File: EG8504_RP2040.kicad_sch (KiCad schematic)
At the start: 1 part, among them U1 RP2040

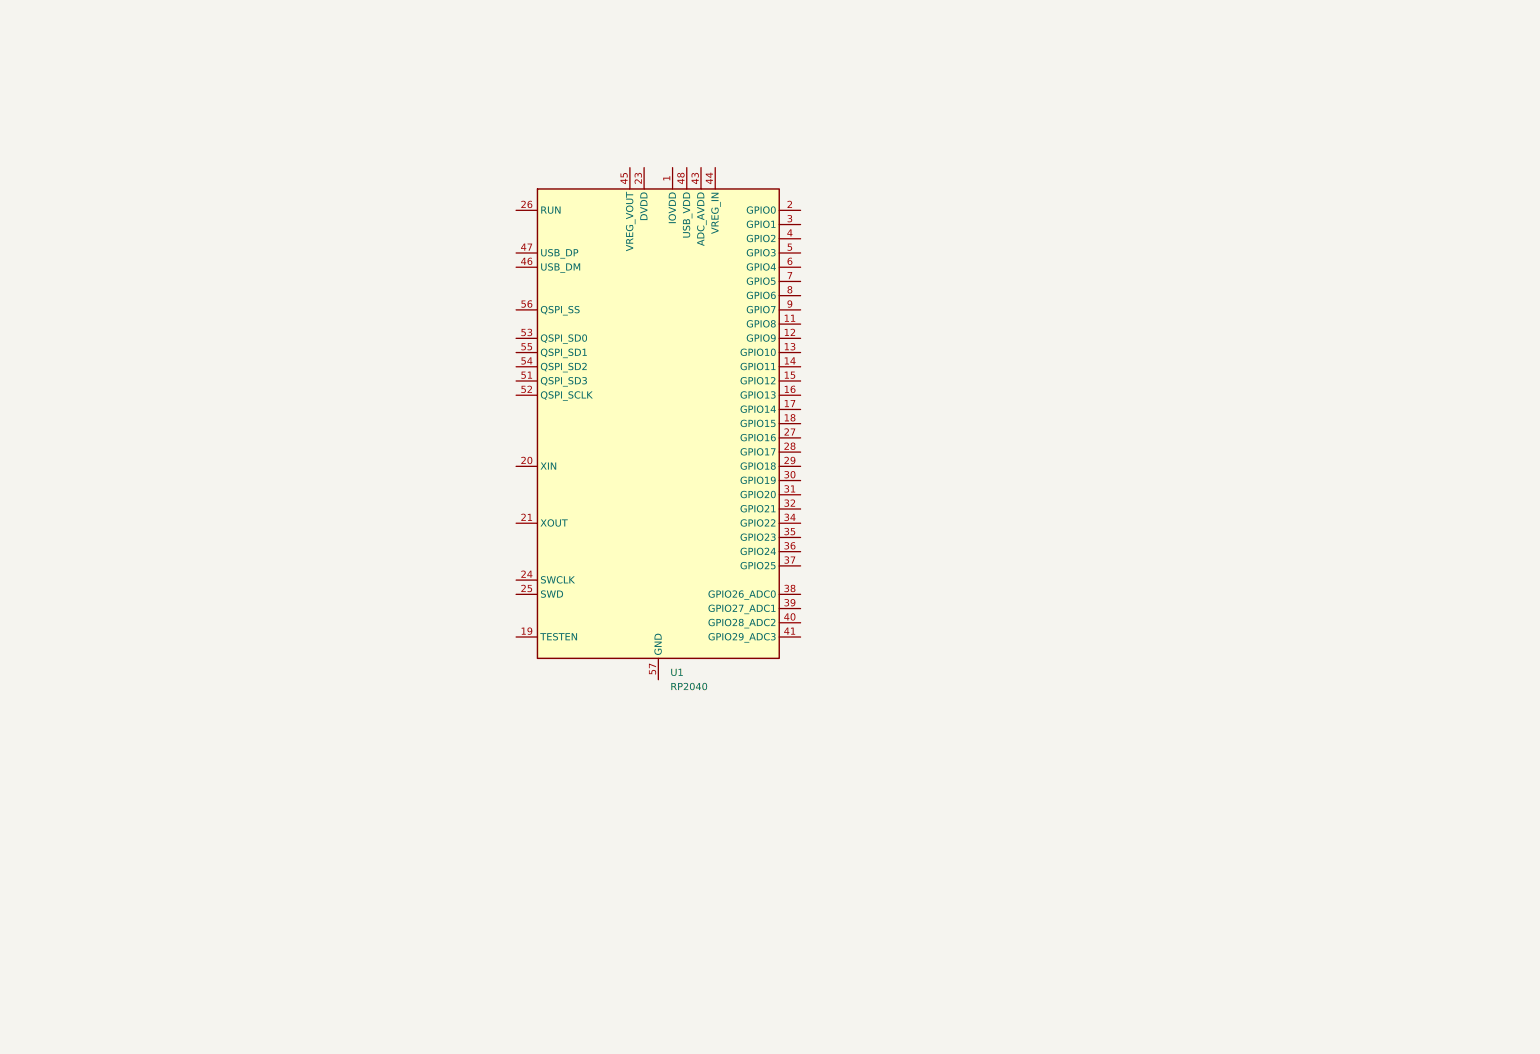
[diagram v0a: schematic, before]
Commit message: rp2040周りの部品配線を追加
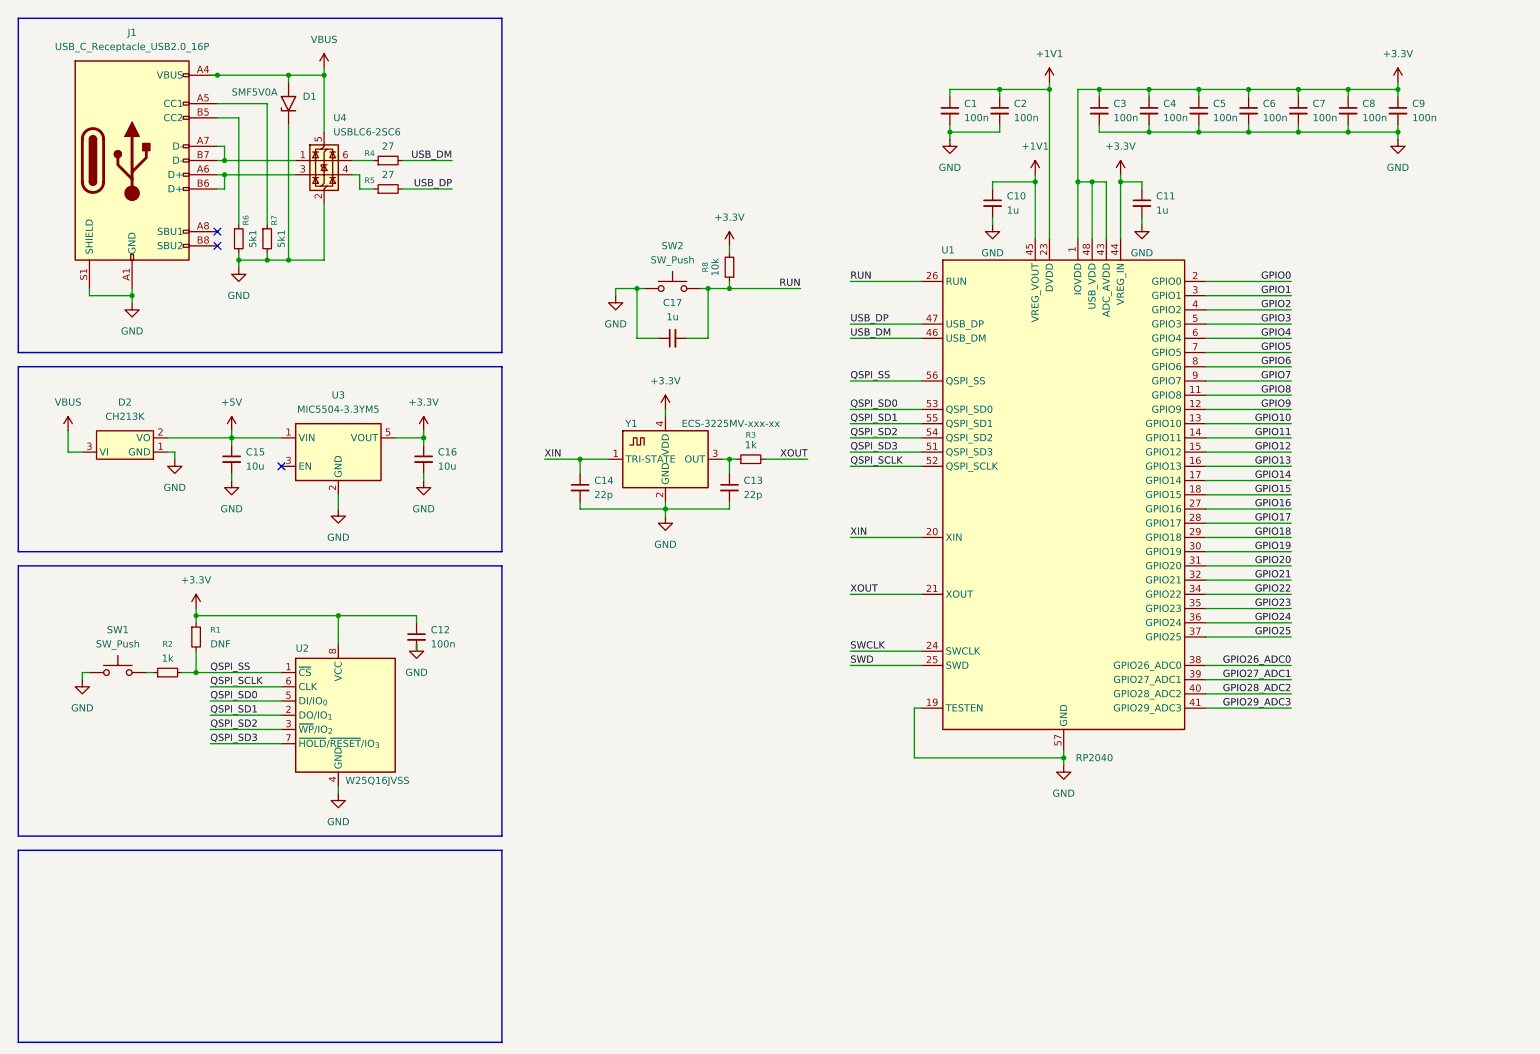
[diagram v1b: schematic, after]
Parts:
- added C1, C12, C2, C3, C4, C5, C6, C7, C8, C9: 100n, symbol Device:C_Small
- added C10, C11, C17: 1u, symbol Device:C_Small
- added C13, C14: 22p, symbol Device:C_Small
- added C15, C16: 10u, symbol Device:C_Small
- added D1: SMF5V0A, Diode_SMD:D_SMF, symbol Diode:SMF5V0A
- added D2: CH213K, symbol MyLibrary:CH213K
- added J1: USB_C_Receptacle_USB2.0_16P, symbol Connector:USB_C_Receptacle_USB2.0_16P
- added R1: DNF, symbol Device:R_Small
- added R2, R3: 1k, symbol Device:R_Small
- added R4, R5: 27, symbol Device:R_Small
- added R6, R7: 5k1, symbol Device:R_Small
- added R8: 10k, symbol Device:R_Small
- added SW1, SW2: SW_Push, symbol Switch:SW_Push
- added U2: W25Q16JVSS, Package_SO:SOIC-8_5.3x5.3mm_P1.27mm, symbol Memory_Flash:W25Q16JVSS
- added U3: MIC5504-3.3YM5, Package_TO_SOT_SMD:SOT-23-5, symbol Regulator_Linear:MIC5504-3.3YM5
- added U4: USBLC6-2SC6, Package_TO_SOT_SMD:SOT-23-6, symbol Power_Protection:USBLC6-2SC6
- added Y1: ECS-3225MV-xxx-xx, symbol MyLibrary:ECS-3225MV-xxx-xx
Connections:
- net +3.3V: now reaches U1.1 (IOVDD), U1.10 (IOVDD), U1.22 (IOVDD), U1.33 (IOVDD), U1.42 (IOVDD), U1.49 (IOVDD)
- net +3.3V: now also U1.43 (ADC_AVDD), U1.44 (VREG_IN), U1.48 (USB_VDD), C11.1, C12.1, C16.1, C3.1, C4.1, C5.1, C6.1, C7.1, C8.1, C9.1, R1.1, R8.2, U2.8 (VCC), U3.5 (VOUT), Y1.4 (VDD)
- net GPIO8: now reaches U1.11 (GPIO8)
- net GPIO9: now reaches U1.12 (GPIO9)
- net GPIO10: now reaches U1.13 (GPIO10)
- net GPIO11: now reaches U1.14 (GPIO11)
- net GPIO12: now reaches U1.15 (GPIO12)
- net GPIO13: now reaches U1.16 (GPIO13)
- net GPIO14: now reaches U1.17 (GPIO14)
- net GPIO15: now reaches U1.18 (GPIO15)
- net GND: now reaches U1.19 (TESTEN)
- net GND: now also U1.57 (GND), C1.2, C10.2, C11.2, C12.2, C13.2, C14.2, C15.2, C16.2, C17.1, C2.2, C3.2, C4.2, C5.2, C6.2, C7.2, C8.2, C9.2, D1.1 (A1), D2.1 (GND), J1.A1 (GND), J1.A12 (GND), J1.B1 (GND), J1.B12 (GND), J1.S1 (SHIELD), R6.2, R7.2, SW1.1, SW2.1, U2.4 (GND), U3.2 (GND), U4.2 (GND), Y1.2 (GND)
- net GPIO0: now reaches U1.2 (GPIO0)
- net XIN: now reaches U1.20 (XIN)
- net XIN: now also C14.1, Y1.1 (TRI-STATE)
- net XOUT: now reaches U1.21 (XOUT)
- net XOUT: now also R3.2
- net +1V1: now reaches U1.23 (DVDD), U1.50 (DVDD)
- net +1V1: now also U1.45 (VREG_VOUT), C1.1, C10.1, C2.1
- net SWCLK: now reaches U1.24 (SWCLK)
- net SWD: now reaches U1.25 (SWD)
- net RUN: now reaches U1.26 (RUN)
- net RUN: now also C17.2, R8.1, SW2.2
- net GPIO16: now reaches U1.27 (GPIO16)
- net GPIO17: now reaches U1.28 (GPIO17)
- net GPIO18: now reaches U1.29 (GPIO18)
- net GPIO1: now reaches U1.3 (GPIO1)
- net GPIO19: now reaches U1.30 (GPIO19)
- net GPIO20: now reaches U1.31 (GPIO20)
- net GPIO21: now reaches U1.32 (GPIO21)
- net GPIO22: now reaches U1.34 (GPIO22)
- net GPIO23: now reaches U1.35 (GPIO23)
- net GPIO24: now reaches U1.36 (GPIO24)
- net GPIO25: now reaches U1.37 (GPIO25)
- net GPIO26_ADC0: now reaches U1.38 (GPIO26_ADC0)
- net GPIO27_ADC1: now reaches U1.39 (GPIO27_ADC1)
- net GPIO2: now reaches U1.4 (GPIO2)
- net GPIO28_ADC2: now reaches U1.40 (GPIO28_ADC2)
- net GPIO29_ADC3: now reaches U1.41 (GPIO29_ADC3)
- net USB_DM: now reaches U1.46 (USB_DM)
- net USB_DM: now also R4.2
- net USB_DP: now reaches U1.47 (USB_DP)
- net USB_DP: now also R5.2
- net GPIO3: now reaches U1.5 (GPIO3)
- net QSPI_SD3: now reaches U1.51 (QSPI_SD3)
- net QSPI_SD3: now also U2.7 (~{HOLD}/~{RESET}/IO_{3})
- net QSPI_SCLK: now reaches U1.52 (QSPI_SCLK)
- net QSPI_SCLK: now also U2.6 (CLK)
- net QSPI_SD0: now reaches U1.53 (QSPI_SD0)
- net QSPI_SD0: now also U2.5 (DI/IO_{0})
- net QSPI_SD2: now reaches U1.54 (QSPI_SD2)
- net QSPI_SD2: now also U2.3 (~{WP}/IO_{2})
- net QSPI_SD1: now reaches U1.55 (QSPI_SD1)
- net QSPI_SD1: now also U2.2 (DO/IO_{1})
- net QSPI_SS: now reaches U1.56 (QSPI_SS)
- net QSPI_SS: now also R1.2, R2.2, U2.1 (~{CS})
- net GPIO4: now reaches U1.6 (GPIO4)
- net GPIO5: now reaches U1.7 (GPIO5)
- net GPIO6: now reaches U1.8 (GPIO6)
- net GPIO7: now reaches U1.9 (GPIO7)
- new net: C13.1, R3.1, Y1.3 (OUT)
- new net: R2.1, SW1.2
- new net: J1.A7 (D-), J1.B7 (D-), U4.1 (I/O1)
- new net: J1.A6 (D+), J1.B6 (D+), U4.3 (I/O2)
- new net: R5.1, U4.4 (I/O2)
- new net: R4.1, U4.6 (I/O1)
- new net: J1.A5 (CC1), R7.1
- new net: J1.B5 (CC2), R6.1
- new net +5V: C15.1, D2.2 (VO), U3.1 (VIN)
- new net VBUS: D1.2 (A2), D2.3 (VI), J1.A4 (VBUS), J1.A9 (VBUS), J1.B4 (VBUS), J1.B9 (VBUS), U4.5 (VBUS)
- no-connect marks 0 -> 3
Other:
- moved on the sheet: U1

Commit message: EG8504用のDCDCを追加
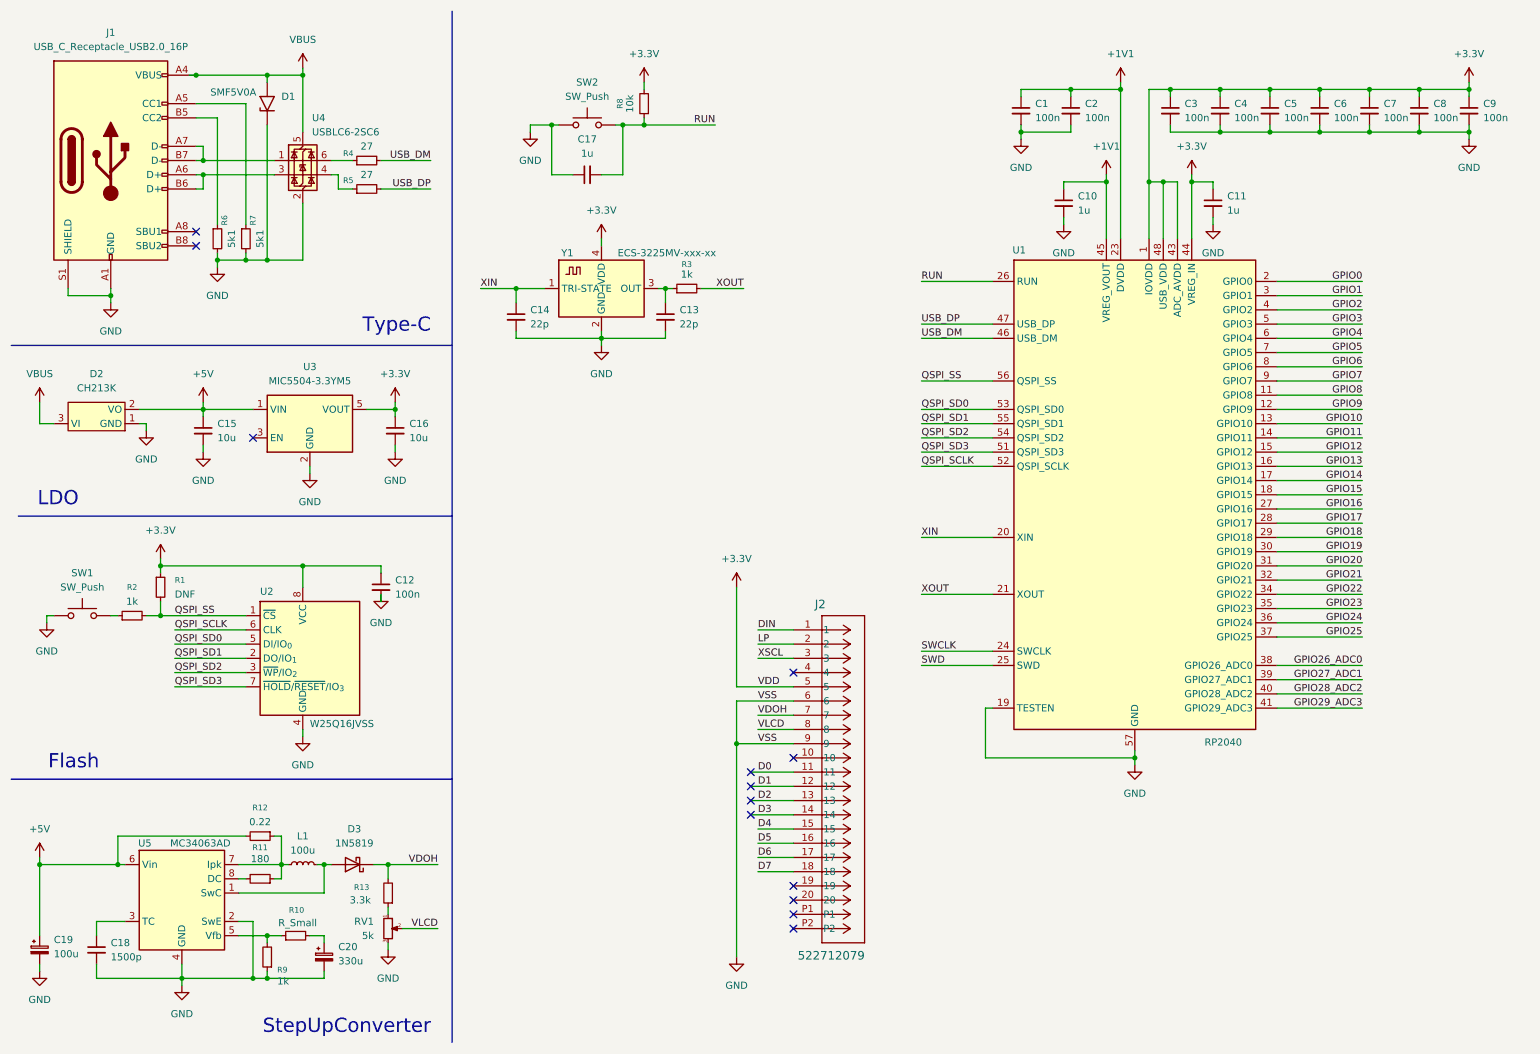
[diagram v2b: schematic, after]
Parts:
- added C18: 1500p, symbol Device:C_Small
- added C19: 100u, symbol Device:C_Polarized_Small
- added C20: 330u, symbol Device:C_Polarized_Small
- added D3: 1N5819, Diode_THT:D_DO-41_SOD81_P10.16mm_Horizontal, symbol Diode:1N5819
- added J2: 522712079, MyLibrary:CON_522712079_MOL, symbol MyLibrary:522712079
- added L1: 100u, symbol Device:L_Small
- added R10: R_Small, symbol Device:R_Small
- added R11: 180, symbol Device:R_Small
- added R12: 0.22, symbol Device:R_Small
- added R13: 3.3k, symbol Device:R_Small
- added R9: 1k, symbol Device:R_Small
- added RV1: 5k, symbol Device:R_Potentiometer_Small
- added U5: MC34063AD, Package_SO:SOIC-8_3.9x4.9mm_P1.27mm, symbol Regulator_Switching:MC34063AD
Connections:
- net +3.3V: now also J2.5
- net +5V: now also C19.1, R12.2, U5.6 (Vin)
- net GND: now also C18.2, C19.2, C20.2, J2.6, J2.9, R9.1, RV1.3, U5.2 (SwE), U5.4 (GND)
- new net: L1.1, R11.1, R12.1, U5.7 (Ipk)
- new net: R11.2, U5.8 (DC)
- new net: D3.2 (A), L1.2, U5.1 (SwC)
- new net: C18.1, U5.3 (TC)
- new net: R10.1, R9.2, U5.5 (Vfb)
- new net: R13.1, RV1.1
- new net: C20.1, R10.2
- new net D0: J2.11
- new net D1: J2.12
- new net D2: J2.13
- new net D3: J2.14
- new net D4: J2.15
- new net D5: J2.16
- new net D6: J2.17
- new net D7: J2.18
- new net DIN: J2.1
- new net LP: J2.2
- new net VDOH: D3.1 (K), J2.7, R13.2
- new net VLCD: J2.8, RV1.2
- new net XSCL: J2.3
- no-connect marks 3 -> 13
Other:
- note added: "Flash"
- note added: "LDO"
- note added: "StepUpConverter"
- note added: "Type-C"
- moved on the sheet: C1, C10, C11, C12, C13, C14, C15, C16, C17, C2, C3, C4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

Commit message: コネクタの配置とPCB
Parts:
- added D4: LED_Small, LED_SMD:LED_0603_1608Metric_Pad1.05x0.95mm_HandSolder, symbol Device:LED_Small
- added J3, J4, J5: Conn_01x03_Socket, Connector_PinHeader_2.54mm:PinHeader_1x03_P2.54mm_Vertical, symbol Connector:Conn_01x03_Socket
- added J6, J7: Conn_01x20_Socket, Connector_PinHeader_2.54mm:PinHeader_1x20_P2.54mm_Vertical, symbol Connector:Conn_01x20_Socket
- added R14: 1k, Resistor_SMD:R_0603_1608Metric_Pad0.98x0.95mm_HandSolder, symbol Device:R_Small
- C1, C10, C11, C12, C13, C14, C15, C16, C17, C18, C2, C3, C4, C5, C6, C7, C8, C9: footprint (none) -> Capacitor_SMD:C_0603_1608Metric_Pad1.08x0.95mm_HandSolder
- C19, C20: footprint (none) -> MyLibrary:CP_Radial_D8.0mm_P3.50mm_P5.00mm
- D2: footprint (none) -> Package_TO_SOT_SMD:SOT-23_Handsoldering
- J1: footprint (none) -> Connector_USB:USB_C_Receptacle_GCT_USB4105-xx-A_16P_TopMnt_Horizontal
- R1, R11, R12, R13, R2, R3, R4, R5, R6, R7, R8, R9: footprint (none) -> Resistor_SMD:R_0603_1608Metric_Pad0.98x0.95mm_HandSolder
- R10: value R_Small -> 15k; footprint (none) -> Resistor_SMD:R_0603_1608Metric_Pad0.98x0.95mm_HandSolder
- SW1, SW2: footprint (none) -> Button_Switch_SMD:SW_Push_1P1T_NO_Vertical_Wuerth_434133025816
- Y1: footprint (none) -> Crystal:Crystal_SMD_3225-4Pin_3.2x2.5mm_HandSoldering
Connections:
- net +3.3V: now also J4.3 (Pin_3), J7.2 (Pin_2)
- net +5V: now also J4.1 (Pin_1), J7.1 (Pin_1)
- net GND: now also J3.2 (Pin_2), J4.2 (Pin_2), J5.2 (Pin_2), J6.13 (Pin_13), J6.18 (Pin_18), J6.3 (Pin_3), J7.13 (Pin_13), J7.18 (Pin_18), J7.3 (Pin_3), J7.8 (Pin_8), R14.1
- net GPIO0: now also J3.1 (Pin_1), J6.1 (Pin_1)
- net GPIO1: now also J3.3 (Pin_3), J6.2 (Pin_2)
- net GPIO10: now also J6.14 (Pin_14)
- net GPIO11: now also J6.15 (Pin_15)
- net GPIO12: now also J6.16 (Pin_16)
- net GPIO13: now also J6.17 (Pin_17)
- net GPIO14: now also J6.19 (Pin_19)
- net GPIO15: now also J6.20 (Pin_20)
- net GPIO16: now also J7.20 (Pin_20)
- net GPIO17: now also J7.19 (Pin_19)
- net GPIO18: now also J7.17 (Pin_17)
- net GPIO19: now also J7.16 (Pin_16)
- net GPIO2: now also J6.4 (Pin_4)
- net GPIO20: now also J7.15 (Pin_15)
- net GPIO21: now also J7.14 (Pin_14)
- net GPIO22: now also J7.12 (Pin_12)
- net GPIO23: now also J7.11 (Pin_11)
- net GPIO24: now also J7.10 (Pin_10)
- net GPIO25: now also D4.2 (A), J7.9 (Pin_9)
- net GPIO26_ADC0: now also J7.7 (Pin_7)
- net GPIO27_ADC1: now also J7.6 (Pin_6)
- net GPIO28_ADC2: now also J7.5 (Pin_5)
- net GPIO29_ADC3: now also J7.4 (Pin_4)
- net GPIO3: now also J6.5 (Pin_5)
- net GPIO4: now also J6.6 (Pin_6)
- net GPIO5: now also J6.7 (Pin_7)
- net GPIO6: now also J6.9 (Pin_9)
- net GPIO7: now also J6.10 (Pin_10)
- net GPIO8: now also J6.11 (Pin_11)
- net GPIO9: now also J6.12 (Pin_12)
- net RUN: now also J6.8 (Pin_8)
- net SWCLK: now also J5.3 (Pin_3)
- net SWD: now also J5.1 (Pin_1)
- new net: D4.1 (K), R14.2
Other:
- moved on the sheet: C1, C10, C11, C13, C14, C17, C2, C3, C4, C5, C6, C7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

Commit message: マイコン回りの配線
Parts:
- removed C17: 1u, Capacitor_SMD:C_0603_1608Metric_Pad1.08x0.95mm_HandSolder, symbol Device:C_Small
- removed J4, J5: Conn_01x03_Socket, Connector_PinHeader_2.54mm:PinHeader_1x03_P2.54mm_Vertical, symbol Connector:Conn_01x03_Socket
- removed J6, J7: Conn_01x20_Socket, Connector_PinHeader_2.54mm:PinHeader_1x20_P2.54mm_Vertical, symbol Connector:Conn_01x20_Socket
- added J4, J5: Conn_01x14_Socket, Connector_PinHeader_2.54mm:PinHeader_1x14_P2.54mm_Vertical, symbol Connector:Conn_01x14_Socket
- C19: footprint MyLibrary:CP_Radial_D8.0mm_P3.50mm_P5.00mm -> Capacitor_SMD:CP_Elec_6.3x5.4
- C20: footprint MyLibrary:CP_Radial_D8.0mm_P3.50mm_P5.00mm -> Capacitor_SMD:CP_Elec_10x10.5
- R1: now not fitted
- RV1: footprint (none) -> Potentiometer_THT:Potentiometer_Vishay_T73YP_Vertical
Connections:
- net GPIO13 is gone; now on net DIN: U1.16 (GPIO13)
- net GPIO16 is gone; now on net D4: U1.27 (GPIO16)
- net GPIO17 is gone; now on net D5: U1.28 (GPIO17)
- net GPIO18 is gone; now on net D6: U1.29 (GPIO18)
- net GPIO19 is gone; now on net D7: U1.30 (GPIO19)
- net LP is gone; now on net GPIO14: J2.2
- net XSCL is gone; now on net GPIO15: J2.3
- net +3.3V: now also J4.1 (Pin_1)
- net +5V: now also J5.1 (Pin_1)
- net GND: now also J5.14 (Pin_14), J5.2 (Pin_2)
- net GPIO0: now also J4.2 (Pin_2); no longer J3.1 (Pin_1)
- net GPIO1: now also J4.3 (Pin_3); no longer J3.3 (Pin_3)
- net GPIO10: now also J4.12 (Pin_12)
- net GPIO11: now also J4.13 (Pin_13)
- net GPIO12: now also J4.14 (Pin_14)
- net GPIO2: now also J4.4 (Pin_4)
- net GPIO20: now also J5.12 (Pin_12)
- net GPIO21: now also J5.11 (Pin_11)
- net GPIO22: now also J5.10 (Pin_10)
- net GPIO23: now also J5.9 (Pin_9)
- net GPIO24: now also J5.8 (Pin_8)
- net GPIO25: now also J5.7 (Pin_7)
- net GPIO26_ADC0: now also J5.6 (Pin_6)
- net GPIO27_ADC1: now also J5.5 (Pin_5)
- net GPIO28_ADC2: now also J5.4 (Pin_4)
- net GPIO29_ADC3: now also J5.3 (Pin_3)
- net GPIO3: now also J4.5 (Pin_5)
- net GPIO4: now also J4.6 (Pin_6)
- net GPIO5: now also J4.7 (Pin_7)
- net GPIO6: now also J4.8 (Pin_8)
- net GPIO7: now also J4.9 (Pin_9)
- net GPIO8: now also J4.10 (Pin_10)
- net GPIO9: now also J4.11 (Pin_11)
- net RUN: now also J5.13 (Pin_13)
- net SWCLK: now also J3.3 (Pin_3)
- net SWD: now also J3.1 (Pin_1)
- net VDOH: now also C20.1, R10.2
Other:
- moved on the sheet: C13, C14, D4, J2, R14, R3, Y1
